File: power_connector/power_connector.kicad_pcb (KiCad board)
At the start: 2 copper layers, 2 parts, among them J1 Conn_01x04_Socket, J2 Conn_01x02_Pin

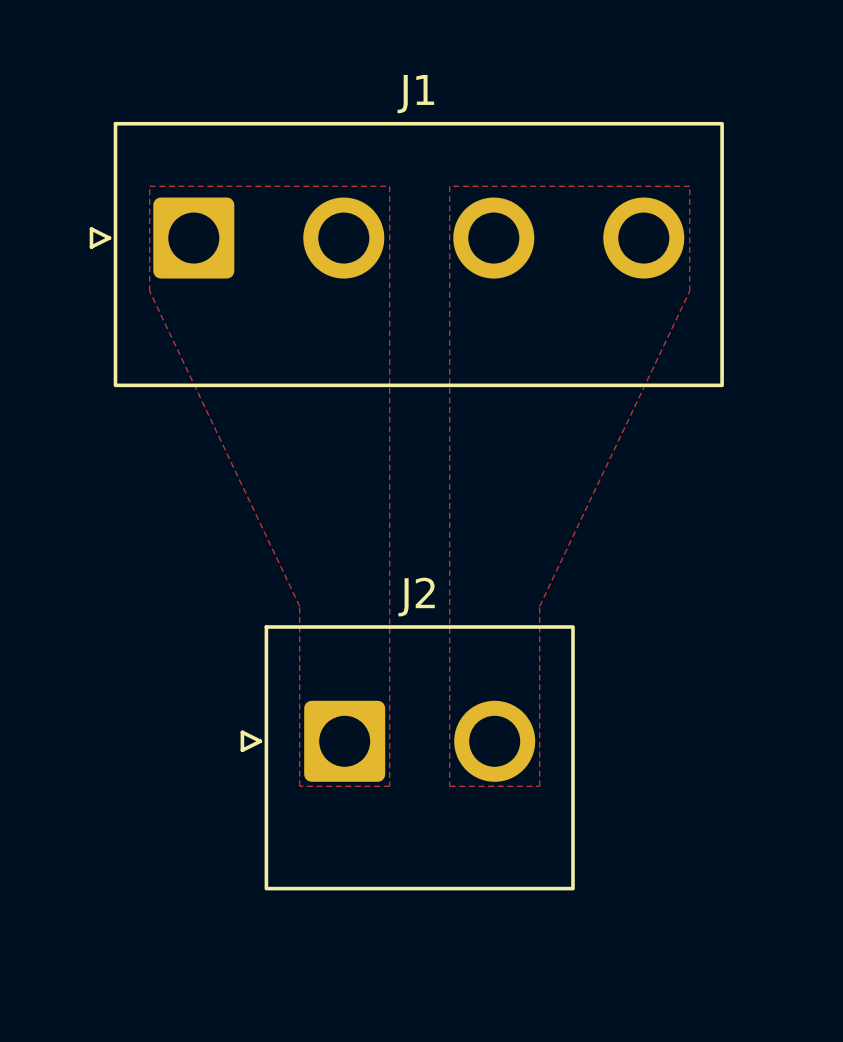
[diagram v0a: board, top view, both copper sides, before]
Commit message: mounting holes and board outline
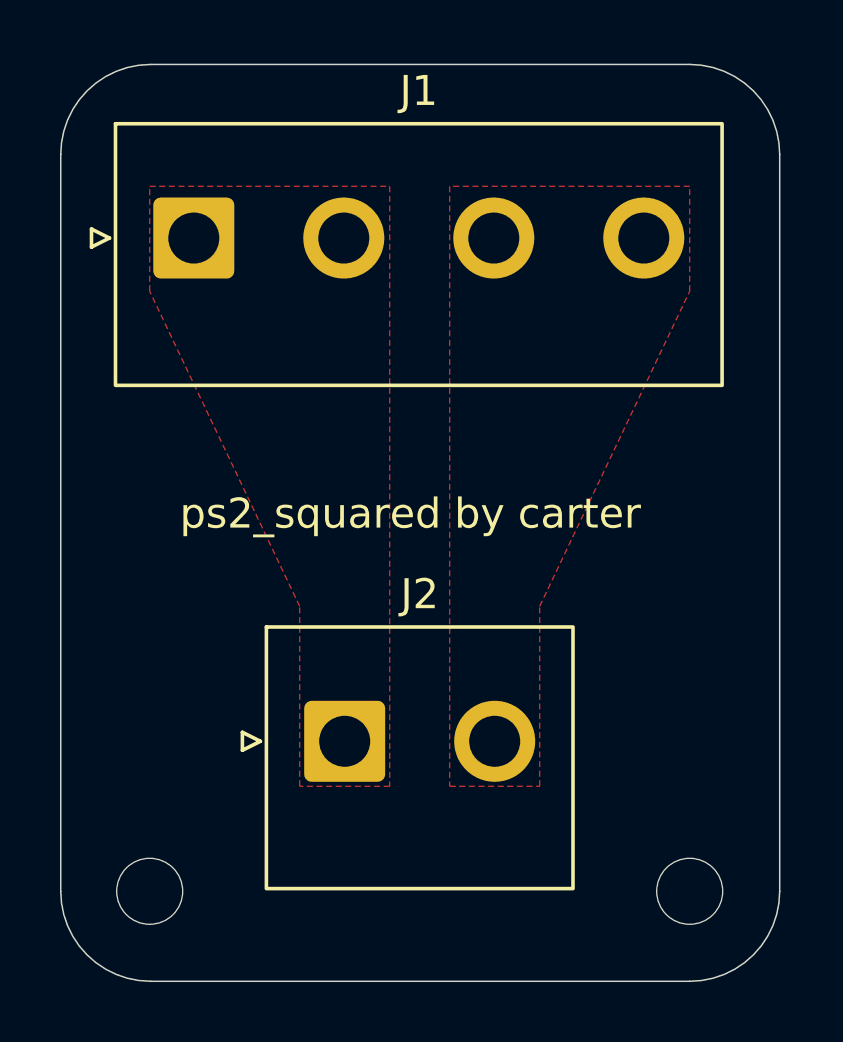
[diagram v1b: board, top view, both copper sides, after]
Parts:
- added H1: MountingHole, MountingHole:MountingHole_2.2mm_M2, F.Cu at (140.5, 120.0)
- added H2: MountingHole, MountingHole:MountingHole_2.2mm_M2, F.Cu at (158.5, 120.0)
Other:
- board outline added: 24 x 30.6 mm
- board text added: "ps2_squared by carter"
